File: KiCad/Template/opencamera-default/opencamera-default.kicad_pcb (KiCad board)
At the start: 4 copper layers, 101.6 x 63.5 mm, 9 parts, among them P1 CONN_LEFT_TOP, P2 CONN_RIGHT_TOP, P3 CONN_LEFT_BOTTOM, P4 CONN_RIGHT_BOTTOM

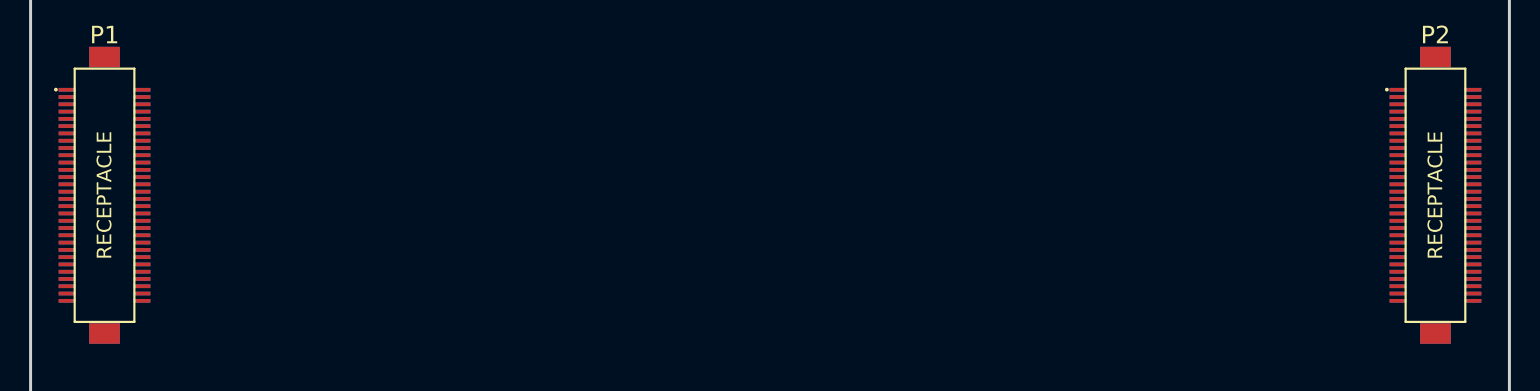
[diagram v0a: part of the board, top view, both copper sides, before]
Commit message: Connected the connectors from front to back on template.
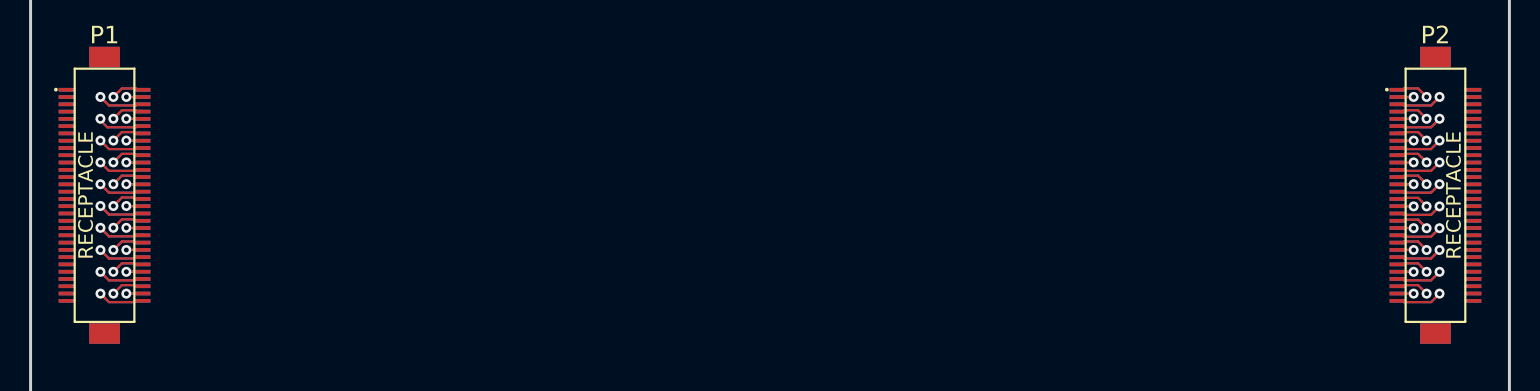
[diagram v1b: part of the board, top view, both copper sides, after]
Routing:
- net /connectors/L6: track 0.00 -> 6.48 mm, vias 0 -> 1
- net /connectors/L3: track 0.00 -> 6.42 mm, vias 0 -> 1
- net /connectors/L27: track 0.00 -> 6.35 mm, vias 0 -> 1
- net /connectors/L21: track 0.00 -> 6.35 mm, vias 0 -> 1
- net /connectors/R18: track 0.00 -> 6.35 mm, vias 0 -> 1
- net /connectors/R21: track 0.00 -> 6.35 mm, vias 0 -> 1
- net /connectors/R24: track 0.00 -> 6.35 mm, vias 0 -> 1
- net /connectors/L24: track 0.00 -> 6.35 mm, vias 0 -> 1
- net /connectors/R27: track 0.00 -> 6.34 mm, vias 0 -> 1
- net /connectors/L30: track 0.00 -> 6.34 mm, vias 0 -> 1
- net /connectors/R30: track 0.00 -> 6.34 mm, vias 0 -> 1
- net /connectors/R3: track 0.00 -> 6.33 mm, vias 0 -> 1
- net /connectors/R6: track 0.00 -> 6.33 mm, vias 0 -> 1
- net /connectors/R9: track 0.00 -> 6.33 mm, vias 0 -> 1
- net /connectors/L18: track 0.00 -> 6.33 mm, vias 0 -> 1
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
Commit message: Initial Debug Board Draft.
Created & routed the debug board.
Created a stitching via footprint for stitching ground planes.
Edited template board to ground the board-board connectors and add
stitching vias through the mounting pads.
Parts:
- added ?: , OpenCamera:STITCH_VIA, F.Cu at (185.4, 98.5)
- added ?: , OpenCamera:STITCH_VIA, F.Cu at (185.4, 117.4)
- added ?: , OpenCamera:STITCH_VIA, F.Cu at (94.0, 98.5)
- added ?: , OpenCamera:STITCH_VIA, F.Cu at (94.0, 117.4)
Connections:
- P1 pad : (no net) -> GNDD
- P2 pad : (no net) -> GNDA
- P3 pad : (no net) -> GNDD
- P4 pad : (no net) -> GNDA
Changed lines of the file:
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@@
 (kicad_pcb (version 4) (host pcbnew "(2015-04-19 BZR 5613)-product")
   (general
-    (links 178)
-    (no_connects 118)
+    (links 189)
+    (no_connects 122)
     (area 88.798399 76.098399 190.601601 139.801601)
     (thickness 1.6)
@@
     (tracks 579)
     (zones 0)
-    (modules 9)
+    (modules 13)
     (nets 63)
   )
@@
     (1 F_inner.Cu signal hide)
     (2 B_inner.Cu signal hide)
-    (31 B.Cu signal)
+    (31 B.Cu signal hide)
     (32 B.Adhes user)
     (33 F.Adhes user)
@@
     (mod_text_size 1 1)
     (mod_text_width 0.15)
-    (pad_size 6.1 6.1)
-    (pad_drill 3.1)
+    (pad_size 2.1 1.4)
+    (pad_drill 0)
     (pad_to_mask_clearance 0)
     (aux_axis_origin 0 0)
-    (visible_elements 7FFFFF7F)
+    (visible_elements 7FFFFD7F)
     (pcbplotparams
       (layerselection 0x00030_80000001)
@@
     (fp_line (start 2.05 8.7) (end -2.05 8.7) (layer F.SilkS) (width 0.15))
     (fp_line (start -2.05 8.7) (end -2.05 -8.7) (layer F.SilkS) (width 0.15))
-    (pad "" smd rect (at 0 9.5) (size 2.1 1.4) (layers F.Cu F.Paste F.Mask))
+    (pad "" smd rect (at 0 9.5) (size 2.1 1.4) (layers F.Cu F.Paste F.Mask)
+      (net 1 GNDD))
     (pad 1 smd rect (at -2.65 -7.25) (size 1 0.25) (layers F.Cu F.Paste F.Mask)
       (net 1 GNDD))
@@
     (pad 60 smd rect (at 2.65 7.25) (size 1 0.25) (layers F.Cu F.Paste F.Mask)
       (net 31 /connectors/L30))
-    (pad "" smd rect (at 0 -9.5) (size 2.1 1.4) (layers F.Cu F.Paste F.Mask))
+    (pad "" smd rect (at 0 -9.5) (size 2.1 1.4) (layers F.Cu F.Paste F.Mask)
+      (net 1 GNDD))
   )
   (module OpenCamera:DF17_60_HEADER (layer B.Cu)
@@
     )
     (fp_circle (center -3.34 7.26) (end -3.32 7.31) (layer B.SilkS) (width 0.15))
-    (pad "" smd rect (at 0 -9.5 180) (size 2.1 1.4) (layers B.Cu B.Paste B.Mask))
+    (pad "" smd rect (at 0 -9.5 180) (size 2.1 1.4) (layers B.Cu B.Paste B.Mask)
+      (net 1 GNDD))
     (pad 1 smd rect (at -2.575 7.25 180) (size 1.15 0.25) (layers B.Cu B.Paste B.Mask)
       (net 2 /connectors/L1))
@@
     (pad 60 smd rect (at 2.575 -7.25 180) (size 1.15 0.25) (layers B.Cu B.Paste B.Mask)
       (net 1 GNDD))
-    (pad "" smd rect (at 0 9.5 180) (size 2.1 1.4) (layers B.Cu B.Paste B.Mask))
+    (pad "" smd rect (at 0 9.5 180) (size 2.1 1.4) (layers B.Cu B.Paste B.Mask)
+      (net 1 GNDD))
   )
   (module OpenCamera:DF17_60_RECEPTACLE (layer F.Cu)
@@
     (fp_line (start 2.05 8.7) (end -2.05 8.7) (layer F.SilkS) (width 0.15))
     (fp_line (start -2.05 8.7) (end -2.05 -8.7) (layer F.SilkS) (width 0.15))
-    (pad "" smd rect (at 0 9.5) (size 2.1 1.4) (layers F.Cu F.Paste F.Mask))
+    (pad GNDA smd rect (at 0 9.5) (size 2.1 1.4) (layers F.Cu F.Paste F.Mask))
     (pad 1 smd rect (at -2.65 -7.25) (size 1 0.25) (layers F.Cu F.Paste F.Mask)
       (net 33 /connectors/R1))
@@
     (pad 60 smd rect (at 2.65 7.25) (size 1 0.25) (layers F.Cu F.Paste F.Mask)
       (net 32 GNDA))
-    (pad "" smd rect (at 0 -9.5) (size 2.1 1.4) (layers F.Cu F.Paste F.Mask))
+    (pad "" smd rect (at 0 -9.5) (size 2.1 1.4) (layers F.Cu F.Paste F.Mask)
+      (net 32 GNDA))
   )
   (module OpenCamera:DF17_60_HEADER (layer B.Cu)
@@
     )
     (fp_circle (center -3.34 7.26) (end -3.32 7.31) (layer B.SilkS) (width 0.15))
-    (pad "" smd rect (at 0 -9.5 180) (size 2.1 1.4) (layers B.Cu B.Paste B.Mask))
+    (pad "" smd rect (at 0 -9.5 180) (size 2.1 1.4) (layers B.Cu B.Paste B.Mask)
+      (net 32 GNDA))
     (pad 1 smd rect (at -2.575 7.25 180) (size 1.15 0.25) (layers B.Cu B.Paste B.Mask)
       (net 32 GNDA))
@@
     (pad 60 smd rect (at 2.575 -7.25 180) (size 1.15 0.25) (layers B.Cu B.Paste B.Mask)
       (net 62 /connectors/R30))
-    (pad "" smd rect (at 0 9.5 180) (size 2.1 1.4) (layers B.Cu B.Paste B.Mask))
+    (pad "" smd rect (at 0 9.5 180) (size 2.1 1.4) (layers B.Cu B.Paste B.Mask)
+      (net 32 GNDA))
+  )
+  (module OpenCamera:STITCH_VIA (layer F.Cu)
+    (at 185.42 98.4504)
+    (fp_text reference "" (at 0 0.5) (layer Eco2.User) hide
+      (effects (font (size 1 1) (thickness 0.15)))
+    )
+    (fp_text value "" (at 0 -0.5) (layer Eco2.User) hide
+      (effects (font (size 1 1) (thickness 0.15)))
+    )
+    (pad "" thru_hole circle (at 0 0) (size 0.6858 0.6858) (drill 0.3302) (layers *.Cu *.Mask F.SilkS)
+      (net 32 GNDA))
+  )
+  (module OpenCamera:STITCH_VIA (layer F.Cu)
+    (at 185.42 117.4496)
+    (fp_text reference "" (at 0 0.5) (layer Eco2.User) hide
+      (effects (font (size 1 1) (thickness 0.15)))
+    )
+    (fp_text value "" (at 0 -0.5) (layer Eco2.User) hide
+      (effects (font (size 1 1) (thickness 0.15)))
+    )
+    (pad "" thru_hole circle (at 0 0) (size 0.6858 0.6858) (drill 0.3302) (layers *.Cu *.Mask F.SilkS)
+      (net 32 GNDA))
+  )
+  (module OpenCamera:STITCH_VIA (layer F.Cu)
+    (at 93.98 98.4504)
+    (fp_text reference "" (at 0 0.5) (layer Eco2.User) hide
+      (effects (font (size 1 1) (thickness 0.15)))
+    )
+    (fp_text value "" (at 0 -0.5) (layer Eco2.User) hide
+      (effects (font (size 1 1) (thickness 0.15)))
+    )
+    (pad "" thru_hole circle (at 0 0) (size 0.6858 0.6858) (drill 0.3302) (layers *.Cu *.Mask F.SilkS)
+      (net 1 GNDD))
+  )
+  (module OpenCamera:STITCH_VIA (layer F.Cu)
+    (at 93.98 117.4496)
+    (fp_text reference "" (at 0 0.5) (layer Eco2.User) hide
+      (effects (font (size 1 1) (thickness 0.15)))
+    )
+    (fp_text value "" (at 0 -0.5) (layer Eco2.User) hide
+      (effects (font (size 1 1) (thickness 0.15)))
+    )
+    (pad "" thru_hole circle (at 0 0) (size 0.6858 0.6858) (drill 0.3302) (layers *.Cu *.Mask F.SilkS)
+      (net 1 GNDD))
   )
   (dimension 63.5 (width 0.3) (layer Eco1.User)

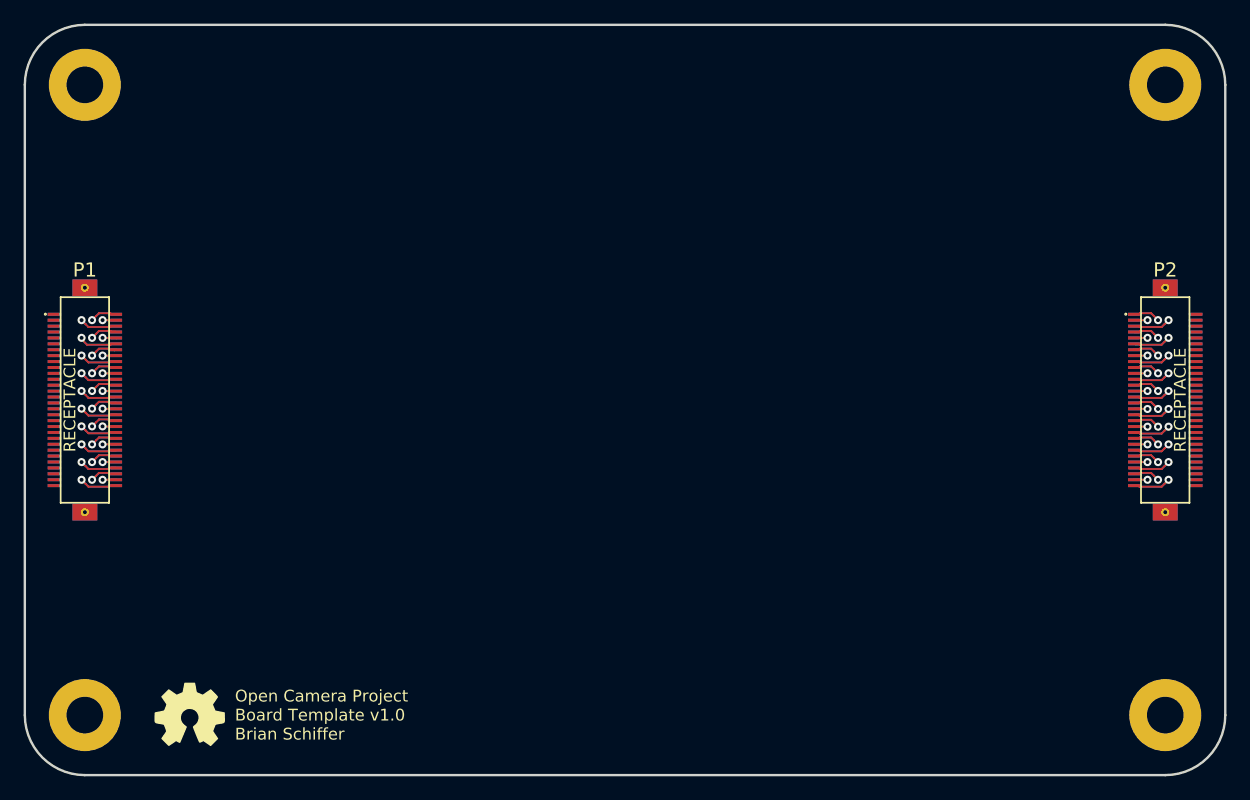
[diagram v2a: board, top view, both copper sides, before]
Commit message: Update Template
v1.1
Removed keepouts around mounting holes (looks nicer).
Modified board-board connectors to include grounded mounting pads with
through via.
Created test point footprints.
Added 1,2,3,4 layer text to confirm proper stackup when receiving from
fab.
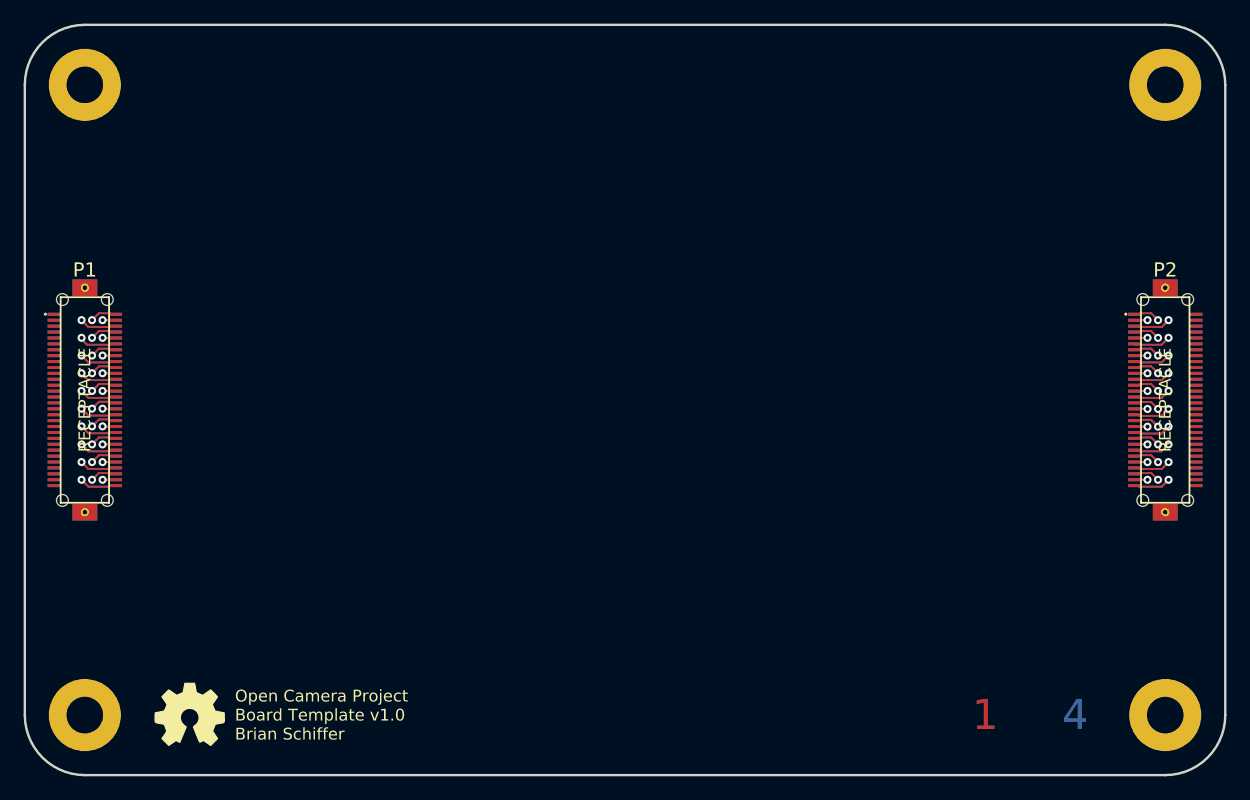
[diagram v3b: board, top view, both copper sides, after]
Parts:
- moved ? 2.26 mm to (187.5, 97.6)
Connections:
- P1 pad : GNDD -> (no net)
- P2 pad : GNDA -> (no net)
- P3 pad : GNDD -> (no net)
- P4 pad : GNDA -> (no net)
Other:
- board text added: "1"
- board text added: "2"
- board text added: "3"
- board text added: "4"

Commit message: Updated Template
-Added default -0.001 paste clearance.
-Added a reference copper pour so I won't have to remember the exact
dimensions away from board edge.
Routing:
- added copper zone on F.Cu, net GNDA
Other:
- board text added: "Open Camera Project Board Template v1.2 Brian Schiffer"
- board text removed: "Open Camera Project Board Template v1.0 Brian Schiffer"

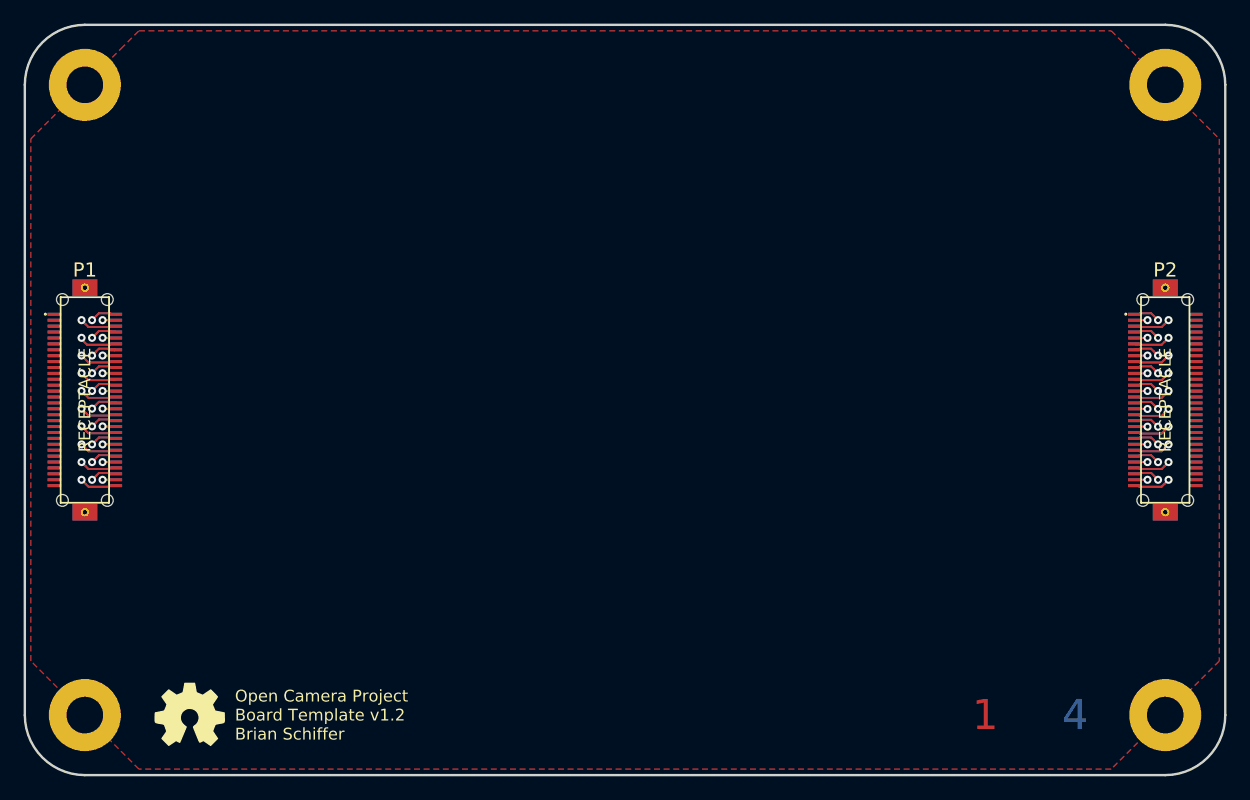
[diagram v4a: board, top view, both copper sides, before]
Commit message: Fixed Template Ground Pour
Now properly uses fillet corners to fully fill the board around mounting
holes. Looks a lot nicer.
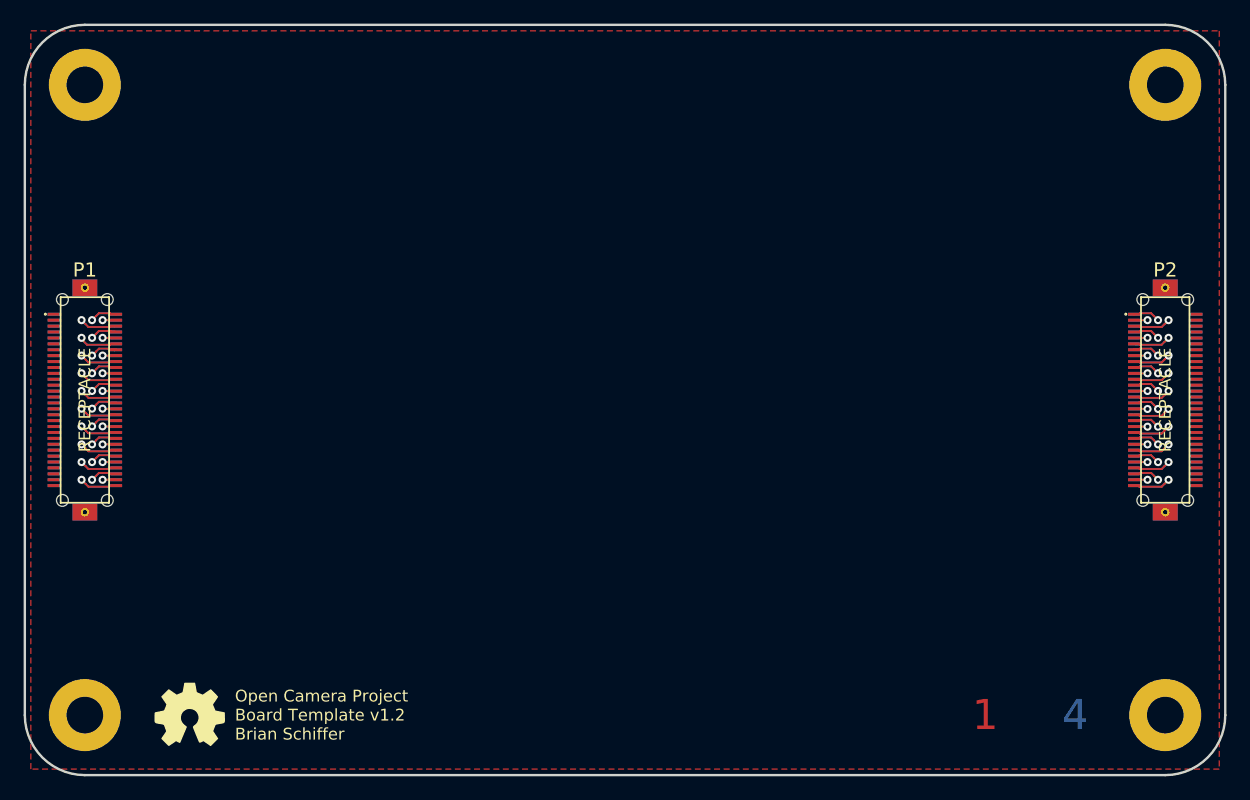
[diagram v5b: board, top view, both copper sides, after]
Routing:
- added copper zone on F.Cu, net GNDD
- removed copper zone on F.Cu, net GNDA
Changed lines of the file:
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@@
   (general
     (links 194)
-    (no_connects 122)
-    (area 84.870456 68.27 202.615715 141.1664)
+    (no_connects 128)
+    (area 88.798399 76.098399 190.601601 139.801601)
     (thickness 1.6)
     (drawings 15)
@@
     )
   )
-  (zone (net 32) (net_name GNDA) (layer F.Cu) (hatch edge 0.508)
+  (zone (net 1) (net_name GNDD) (layer F.Cu) (hatch edge 0.508)
     (connect_pads (clearance 0.1524))
     (min_thickness 0.1524)
-    (fill (arc_segments 16) (thermal_gap 0.1524) (thermal_bridge_width 0.1778))
+    (fill (arc_segments 32) (thermal_gap 0.1524) (thermal_bridge_width 0.1778) (smoothing fillet) (radius 4.572))
     (polygon
       (pts
-        (xy 97.028 78.232) (xy 98.552 76.708) (xy 180.848 76.708) (xy 189.992 85.852) (xy 189.992 130.048)
-        (xy 180.848 139.192) (xy 98.552 139.192) (xy 89.408 130.048) (xy 89.408 85.852) (xy 97.028 78.232)
+        (xy 189.992 139.192) (xy 89.408 139.192) (xy 89.408 76.708) (xy 189.992 76.708)
       )
     )
